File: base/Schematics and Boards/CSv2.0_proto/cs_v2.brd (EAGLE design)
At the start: 44.5 x 44.5 mm, 80 parts, among them J101 J-JTAG-CORTEX-NEEDLE6LEGS, J301 HIROSE-DF40_44-PIN_CONNECTORS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, J302 HIROSE-DF40_30-PIN_CONNECTORS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, Q201 FK3303010L, Q202 DMG3415UFY4Q-7, Q203 FK3303010L, Q204 FK3303010L, U101 ATSAMD51, U102 AT25SF641-MHB-T, U201 COULOMB-MAX17262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

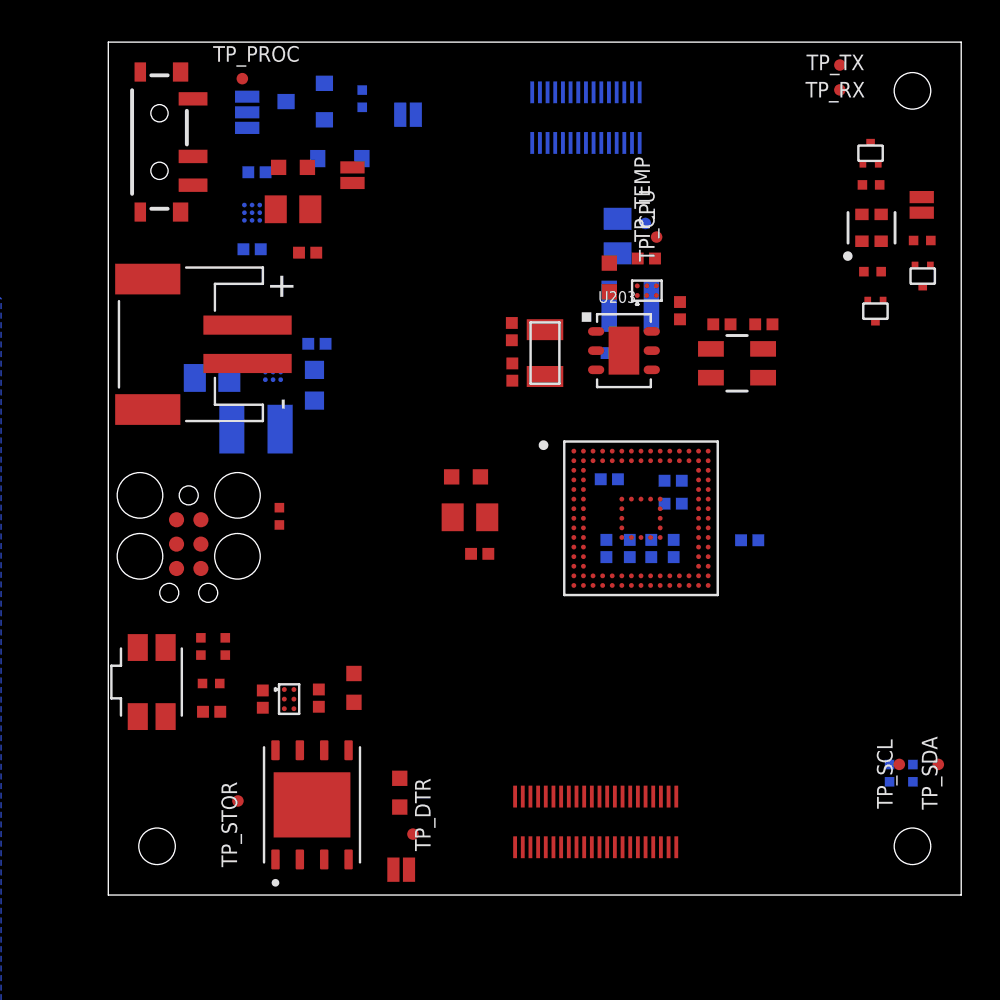
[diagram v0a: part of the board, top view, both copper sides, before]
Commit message: Hand routed power traces, setup DRU
Traces and vias unlocked. No ground planes; just fill.

Most ground traces via'd to let fill easily handle them. Not sure if autoroute will try to route them on their own, but escaping there probably won't be sufficient fill w/i the BGA's area. 

DRU setup for 4mil traces, 6mil vias, no microvias
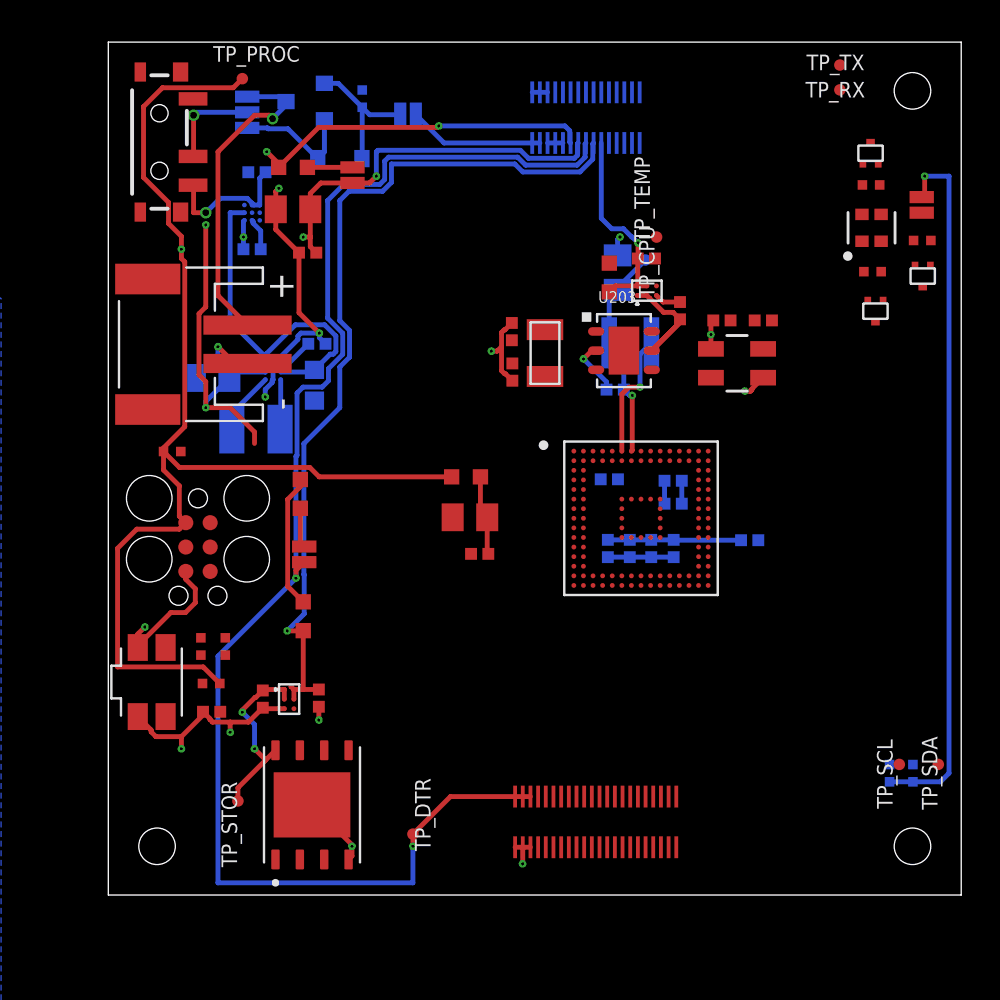
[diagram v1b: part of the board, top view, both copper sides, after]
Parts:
- moved JP205 17.2 mm to (10.2, 17.8), turned to 90 degrees
- moved R207 16.4 mm to (10.0, 20.9)
- moved R106 6.53 mm to (3.33, 23.1), turned to 180 degrees
- moved R208 4.57 mm to (10.2, 14.5)
- moved C103 1.91 mm to (26.4, 26.3)
- moved C107 1.91 mm to (26.5, 32.4)
- moved L101 1.91 mm to (27.2, 28.8)
- moved TP_CPU 1.90 mm to (28.0, 33.1)
- moved J101 0.51 mm to (4.67, 18.1)
- moved C116 0.20 mm to (34.1, 29.9)
- moved C117 0.20 mm to (32.0, 29.9)
- moved C109 0.08 mm to (26.0, 18.1), turned to 270 degrees
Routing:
- net +3V3_PROC: track 0.00 -> 132.5 mm, vias 0 -> 4
- net +3V3_DTR: track 0.00 -> 75.8 mm, vias 0 -> 2
- net GND: track 0.00 -> 60.3 mm, vias 0 -> 16
- net +3V3: track 0.00 -> 49.2 mm, vias 0 -> 4
- net +3V3_STOR_SENSE: track 0.00 -> 45.8 mm, vias 0 -> 1
- net VREG_IN: track 0.00 -> 17.8 mm
- net +3V7_BATT: track 0.00 -> 17.5 mm, vias 0 -> 1
- net VDDCORE: track 0.00 -> 11.3 mm, vias 0 -> 1
- net +3V3_TEMP_SENSE: track 0.00 -> 10.7 mm, vias 0 -> 1
- net +3V3_STOR: track 0.00 -> 9.69 mm, vias 0 -> 2
- net VDD_DBG_JMP: track 0.00 -> 7.31 mm
- net CC_IN: track 0.00 -> 7.27 mm, vias 0 -> 1
- net +3V3_TEMP: track 0.00 -> 7.23 mm
- net VDD_DBG: track 0.00 -> 7.07 mm
- net VSW: track 0.00 -> 6.63 mm, vias 0 -> 1
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
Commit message: Ready to route
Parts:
- moved TP_SDA 30.6 mm to (40.7, 37.3), turned to 90 degrees
- moved TP_SCL 30.5 mm to (43.1, 37.3)
- moved R103 27.4 mm to (42.5, 33.7), flipped to the top
- moved R104 27.3 mm to (40.6, 33.7), flipped to the top
- moved Q201 8.28 mm to (43.1, 24.0)
- moved Q203 8.28 mm to (40.6, 22.2)
- moved R202 8.28 mm to (43.1, 25.9)
- moved R203 8.28 mm to (40.5, 24.2)
- moved R204 8.28 mm to (40.4, 28.8)
- moved JP202 8.28 mm to (43.0, 27.7)
- moved Q204 8.28 mm to (40.4, 30.4)
- moved D202 8.28 mm to (40.4, 26.5)
- moved C106 4.69 mm to (34.1, 19.6)
- moved J301 1.27 mm to (25.4, 5.08)
- moved C104 0.63 mm to (34.1, 18.5)
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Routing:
- net +3V3_PROC: track 132.5 -> 116.3 mm, vias 4 -> 5
- net GND: track 60.3 -> 74.9 mm, vias 16 -> 22
- net VDDANA: track 4.18 -> 16.3 mm, vias 0 -> 3
- net +3V3_DTR: track 75.8 -> 78.2 mm

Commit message: Avoided catastrophe from file inconsistencies
Several hours of nightmare-inducing file-fiddling later...
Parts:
- J101: value J-JTAG-CORTEX-NEEDLE6LEGS -> J-JTAG-CORTEX-NEEDLE6-LEGS
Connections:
- removed net N$1: S201.1
- net CC_IN: no longer S201.1
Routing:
- net CC_IN: track 7.27 -> 5.19 mm
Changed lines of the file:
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@@
 <attribute name="VALUE" x="11.176" y="26.162" size="1.27" layer="27" font="vector" rot="R90"/>
 </element>
-<element name="J101" library="Connectors" package="8.06.16_6-PIN_NEEDLE_ADAPTER_LEGS" value="J-JTAG-CORTEX-NEEDLE6LEGS" x="4.6736" y="18.1356" smashed="yes" rot="R270"/>
+<element name="J101" library="Connectors" package="8.06.16_6-PIN_NEEDLE_ADAPTER_LEGS" value="J-JTAG-CORTEX-NEEDLE6-LEGS" x="4.6736" y="18.1356" smashed="yes" rot="R270"/>
 <element name="JP202" library="Connectors" package="SMT-JUMPER_2_NC_PASTE_NO-SILK" package3d_urn="urn:adsk.eagle:package:39283/1" value="JUMPER-SMT_2_NC_PASTE_NO-SILK" x="43.0276" y="27.7114" smashed="yes" rot="R90">
 <attribute name="BOM" value="EXCLUDE" x="43.0276" y="27.7114" size="1.778" layer="27" rot="R90" display="off"/>
@@
 <contactref element="C201" pad="1"/>
 <contactref element="U201" pad="A1"/>
-<contactref element="S201" pad="1"/>
-<wire x1="4.417" y1="36.993" x2="4.445" y2="36.965" width="0.254" layer="1"/>
-<wire x1="4.445" y1="36.965" x2="4.445" y2="35.56" width="0.254" layer="1"/>
-<wire x1="4.445" y1="35.56" x2="5.08" y2="35.56" width="0.254" layer="1"/>
 <via x="5.08" y="35.56" extent="1-16" drill="0.35"/>
 <wire x1="7.5860125" y1="35.96" x2="7.893" y2="35.96" width="0.254" layer="16"/>
@@
 <signal name="VDD_SW_IN" class="1">
 <contactref element="JP203" pad="2"/>
-<contactref element="S201" pad="2"/>
 <wire x1="7.239" y1="40.7924" x2="4.5974" y2="40.7924" width="0.254" layer="16"/>
 <wire x1="4.5974" y1="40.7924" x2="4.445" y2="40.64" width="0.254" layer="16"/>
@@
 <wire x1="4.445" y1="40.64" x2="4.445" y2="38.521" width="0.254" layer="1"/>
 <wire x1="4.445" y1="38.521" x2="4.417" y2="38.493" width="0.254" layer="1"/>
+<contactref element="S201" pad="2"/>
 </signal>
 <signal name="+3V3_PROC">
@@
 </signal>
 <signal name="N$1">
-<contactref element="S201" pad="1"/>
 </signal>
 </signals>

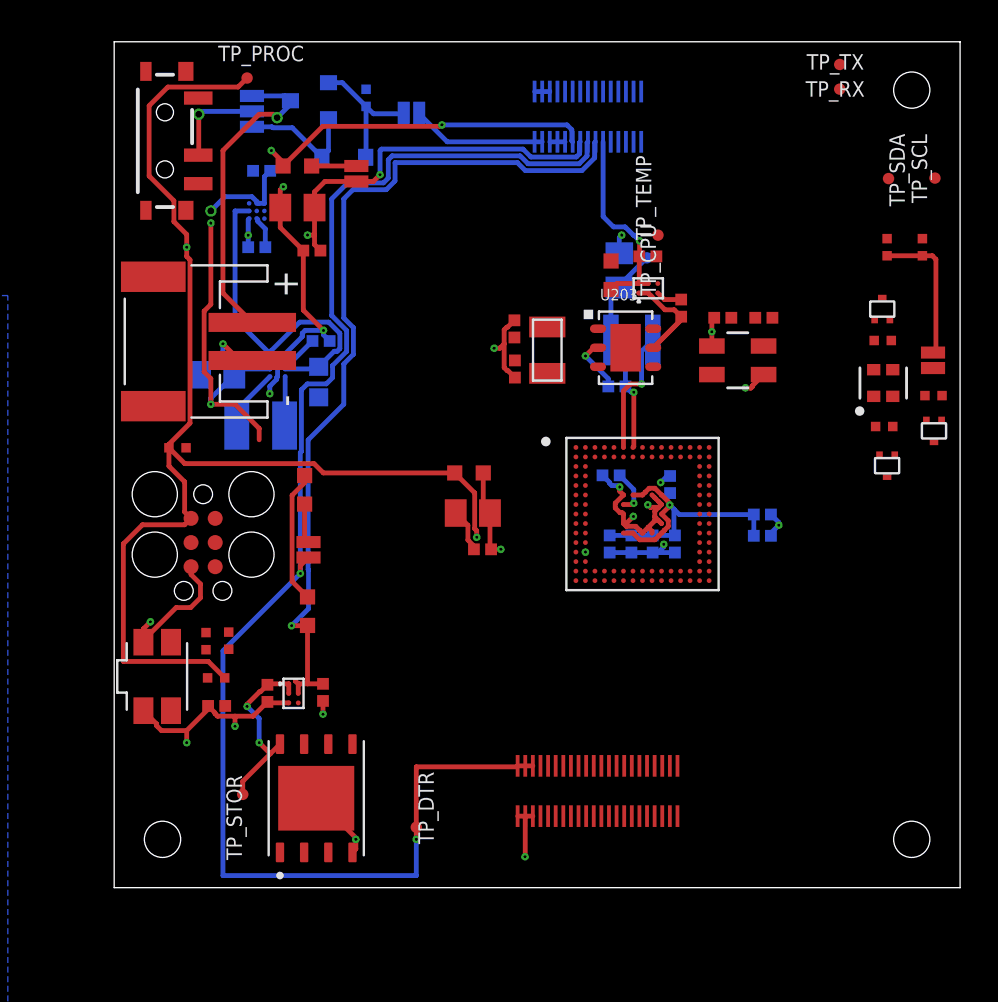
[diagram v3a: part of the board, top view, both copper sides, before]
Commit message: A few small manual routes
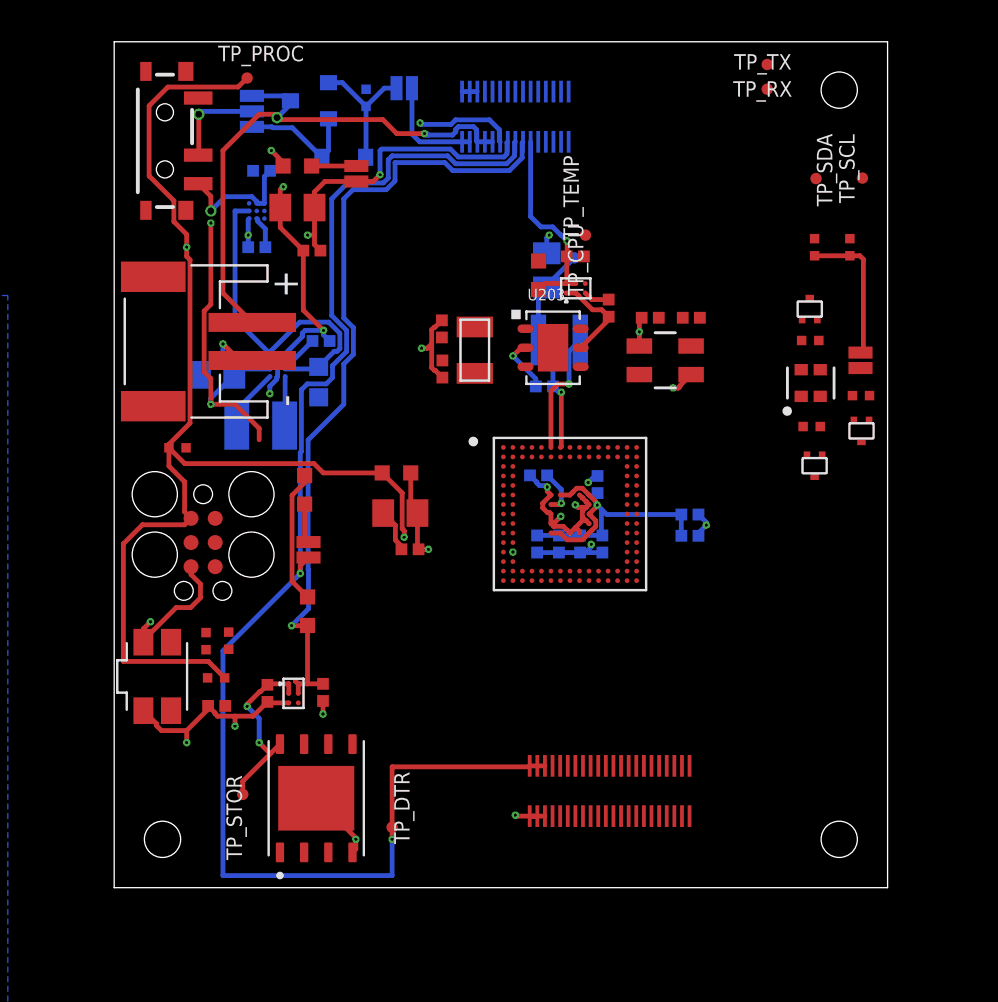
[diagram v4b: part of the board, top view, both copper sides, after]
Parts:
- moved C110 3.81 mm to (15.0, 19.7)
- moved C111 3.81 mm to (23.4, 18.1)
- moved C112 3.81 mm to (25.4, 21.2)
- moved D202 3.81 mm to (36.6, 26.5)
- moved JP202 3.81 mm to (39.2, 27.7)
- moved Q201 3.81 mm to (39.3, 24.0)
- moved Q203 3.81 mm to (36.8, 22.2)
- moved R103 3.81 mm to (38.7, 33.7)
- moved R104 3.81 mm to (36.8, 33.7)
- moved R203 3.81 mm to (36.7, 24.2)
- moved R204 3.81 mm to (36.6, 28.8)
- moved TP_RX 3.81 mm to (34.3, 42.0)
- moved TP_SDA 3.81 mm to (36.9, 37.3)
- moved TP_TX 3.81 mm to (34.3, 43.3)
- moved U203 3.81 mm to (23.1, 28.4)
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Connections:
- net CC_IN: now also S201.1
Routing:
- net +3V7_BATT: track 17.5 -> 29.5 mm, vias 1 -> 2
- net +3V3_PROC: track 116.3 -> 108.7 mm
- net +3V3_STOR_SENSE: track 45.8 -> 42.0 mm
- net +3V3: track 49.2 -> 46.0 mm
- net +3V3_DTR: track 78.2 -> 75.0 mm
- net +3V3_TEMP: track 7.23 -> 4.99 mm
- net CC_IN: track 5.19 -> 6.90 mm
- net VDD_DBG: track 7.07 -> 5.62 mm
- net GND: track 74.9 -> 73.9 mm
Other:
- board size 44.5 x 44.5 mm -> 40.6 x 44.5 mm

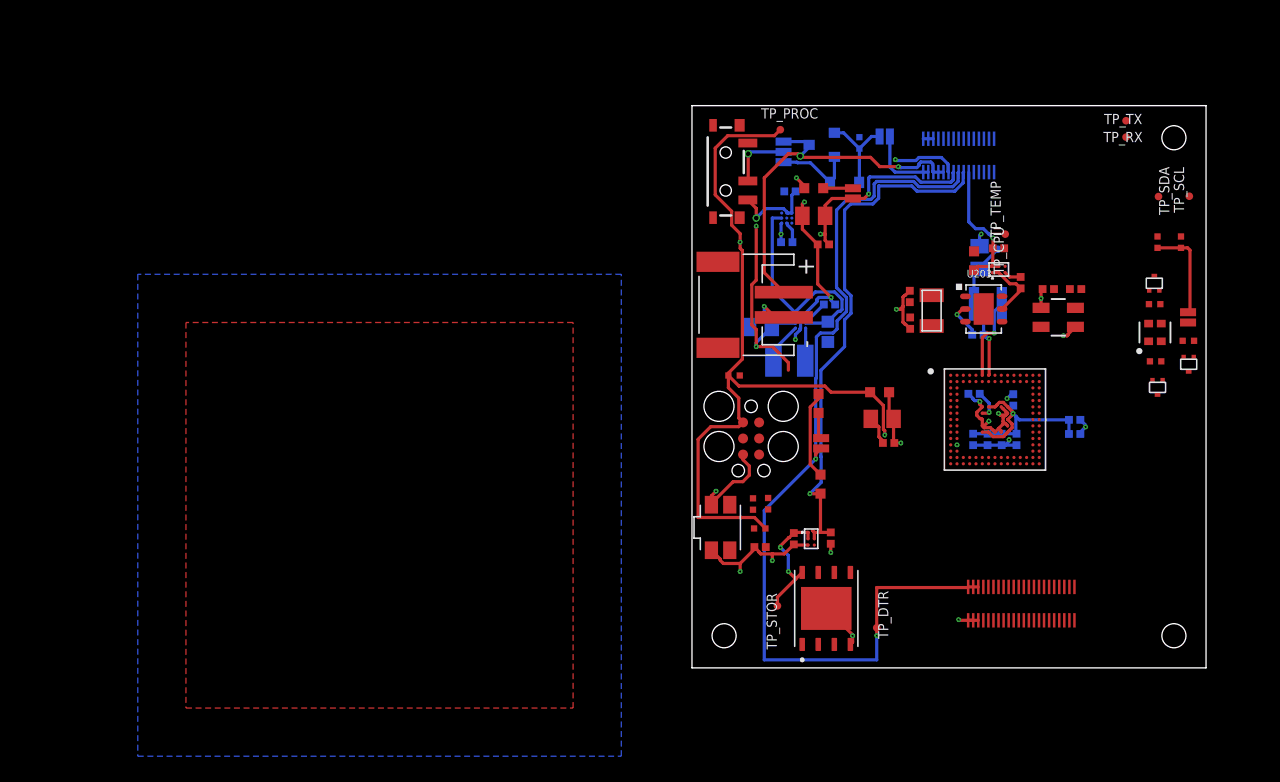
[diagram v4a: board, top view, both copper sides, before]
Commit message: Routed last power traces, made polygon fills
Most of the ground traces are just via'd so that GND fill can pick them up without more traces
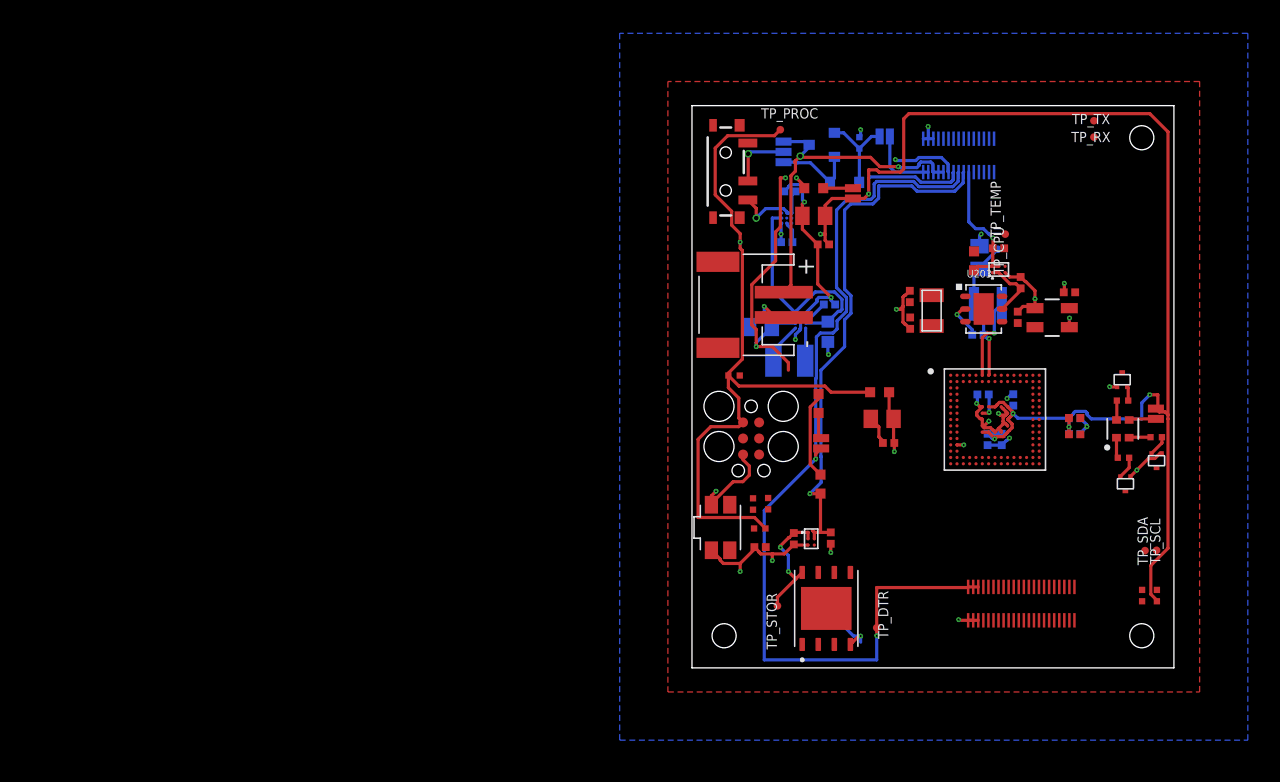
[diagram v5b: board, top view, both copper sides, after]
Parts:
- moved TP_SCL 28.1 mm to (36.7, 9.30)
- moved TP_SDA 28.0 mm to (35.8, 9.27)
- moved R103 28.0 mm to (36.8, 5.71)
- moved R104 28.0 mm to (35.6, 5.71)
- moved C109 8.20 mm to (30.3, 19.8), flipped to the top, turned to 0 degrees
- moved Q204 8.03 mm to (34.0, 22.8)
- moved D202 8.03 mm to (34.1, 18.9)
- moved JP202 8.03 mm to (36.7, 20.1)
- moved Q201 8.03 mm to (36.7, 16.4)
- moved Q203 8.03 mm to (34.3, 14.6)
- moved R203 8.03 mm to (34.1, 16.6)
- moved R204 8.03 mm to (34.0, 21.1)
- moved R202 8.03 mm to (36.7, 18.2)
- moved C102 4.62 mm to (30.3, 18.5), flipped to the top, turned to 0 degrees
- moved C117 3.29 mm to (25.8, 27.7), turned to 90 degrees
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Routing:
- net +3V3_PROC: track 108.7 -> 176.4 mm, vias 5 -> 7
- net GND: track 73.9 -> 86.0 mm, vias 22 -> 28
- net LED_VIN: track 0.00 -> 2.15 mm
- net +3V7_BATT: track 29.5 -> 27.6 mm
- net N$16: track 0.00 -> 1.77 mm
- net N$4: track 0.00 -> 1.71 mm
- net N$12: track 0.00 -> 1.63 mm
- net N$15: track 0.00 -> 1.62 mm
- net N$14: track 0.00 -> 1.55 mm
- net N$17: track 0.00 -> 1.11 mm
- net VDDANA: track 16.3 -> 17.3 mm
- net +3V3: track 46.0 -> 45.5 mm
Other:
- board size 40.6 x 44.5 mm -> 38.1 x 44.5 mm
